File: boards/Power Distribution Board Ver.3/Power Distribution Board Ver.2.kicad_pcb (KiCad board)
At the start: 4 copper layers, 79 parts, among them J1 Screw_Terminal_01x02, J4 Screw_Terminal_01x06, U1 SIC431AED-T1-GE3, U2 SIC431AED-T1-GE3, U3 SIC431AED-T1-GE3

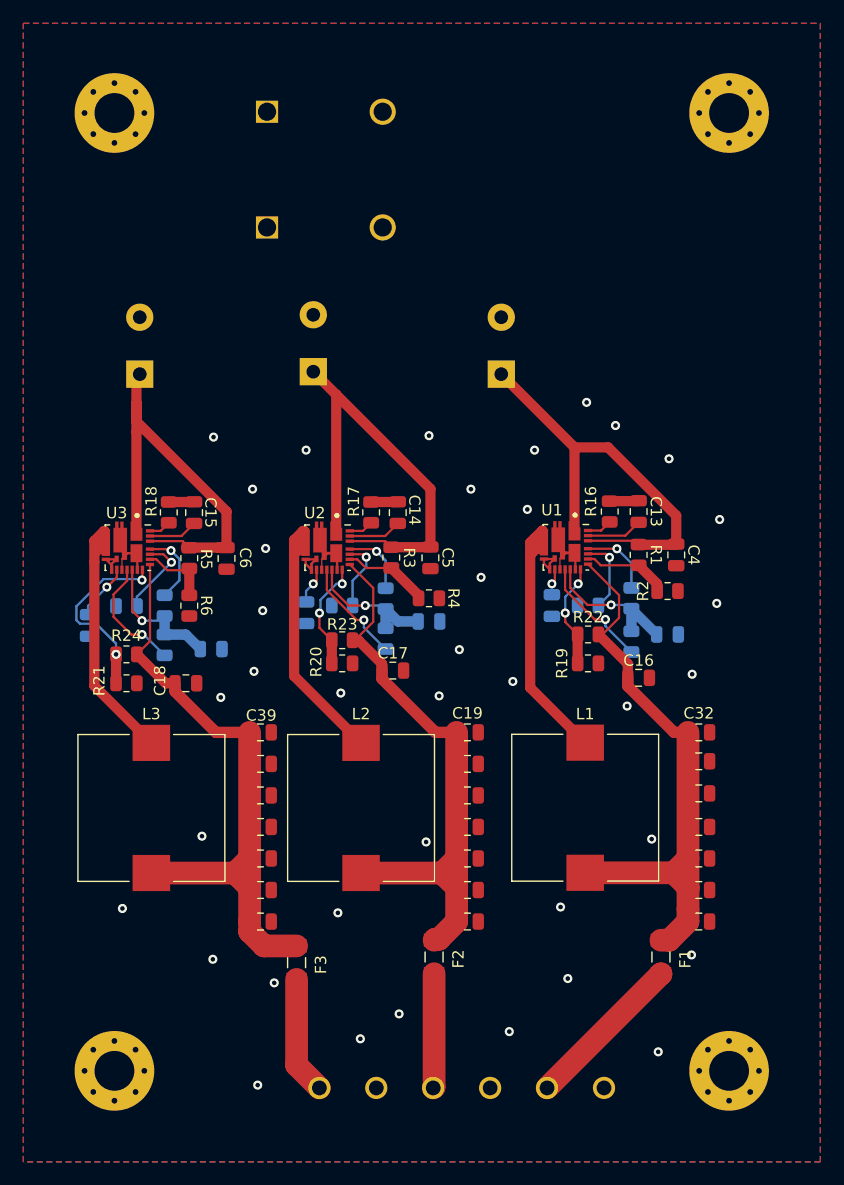
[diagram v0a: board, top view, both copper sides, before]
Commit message: Add edge cuts
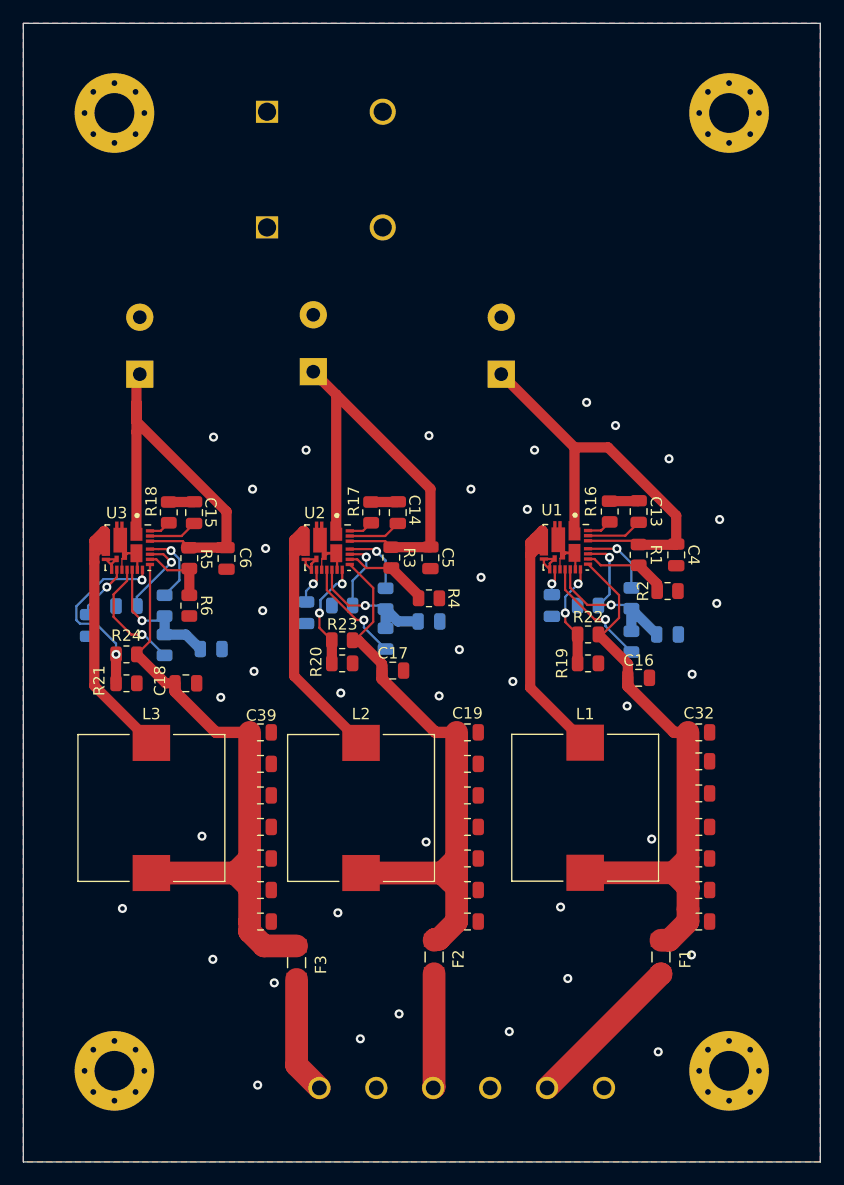
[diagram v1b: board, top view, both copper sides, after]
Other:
- board outline added: 70 x 100 mm
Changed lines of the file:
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@@
 		)
+	)
+	(gr_rect
+		(start 18 23)
+		(end 88 123)
+		(stroke
+			(width 0.1)
+			(type default)
+		)
+		(fill none)
+		(layer "Edge.Cuts")
 	)
 	(gr_text "+"
